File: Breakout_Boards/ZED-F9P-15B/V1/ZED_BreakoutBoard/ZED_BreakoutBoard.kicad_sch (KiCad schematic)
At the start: 15 parts, among them IC1 ZED-F9P-15B, J1 RF2-04A-T-00-50-G, J2 GPS_Conn_02x04_Top_Bottom

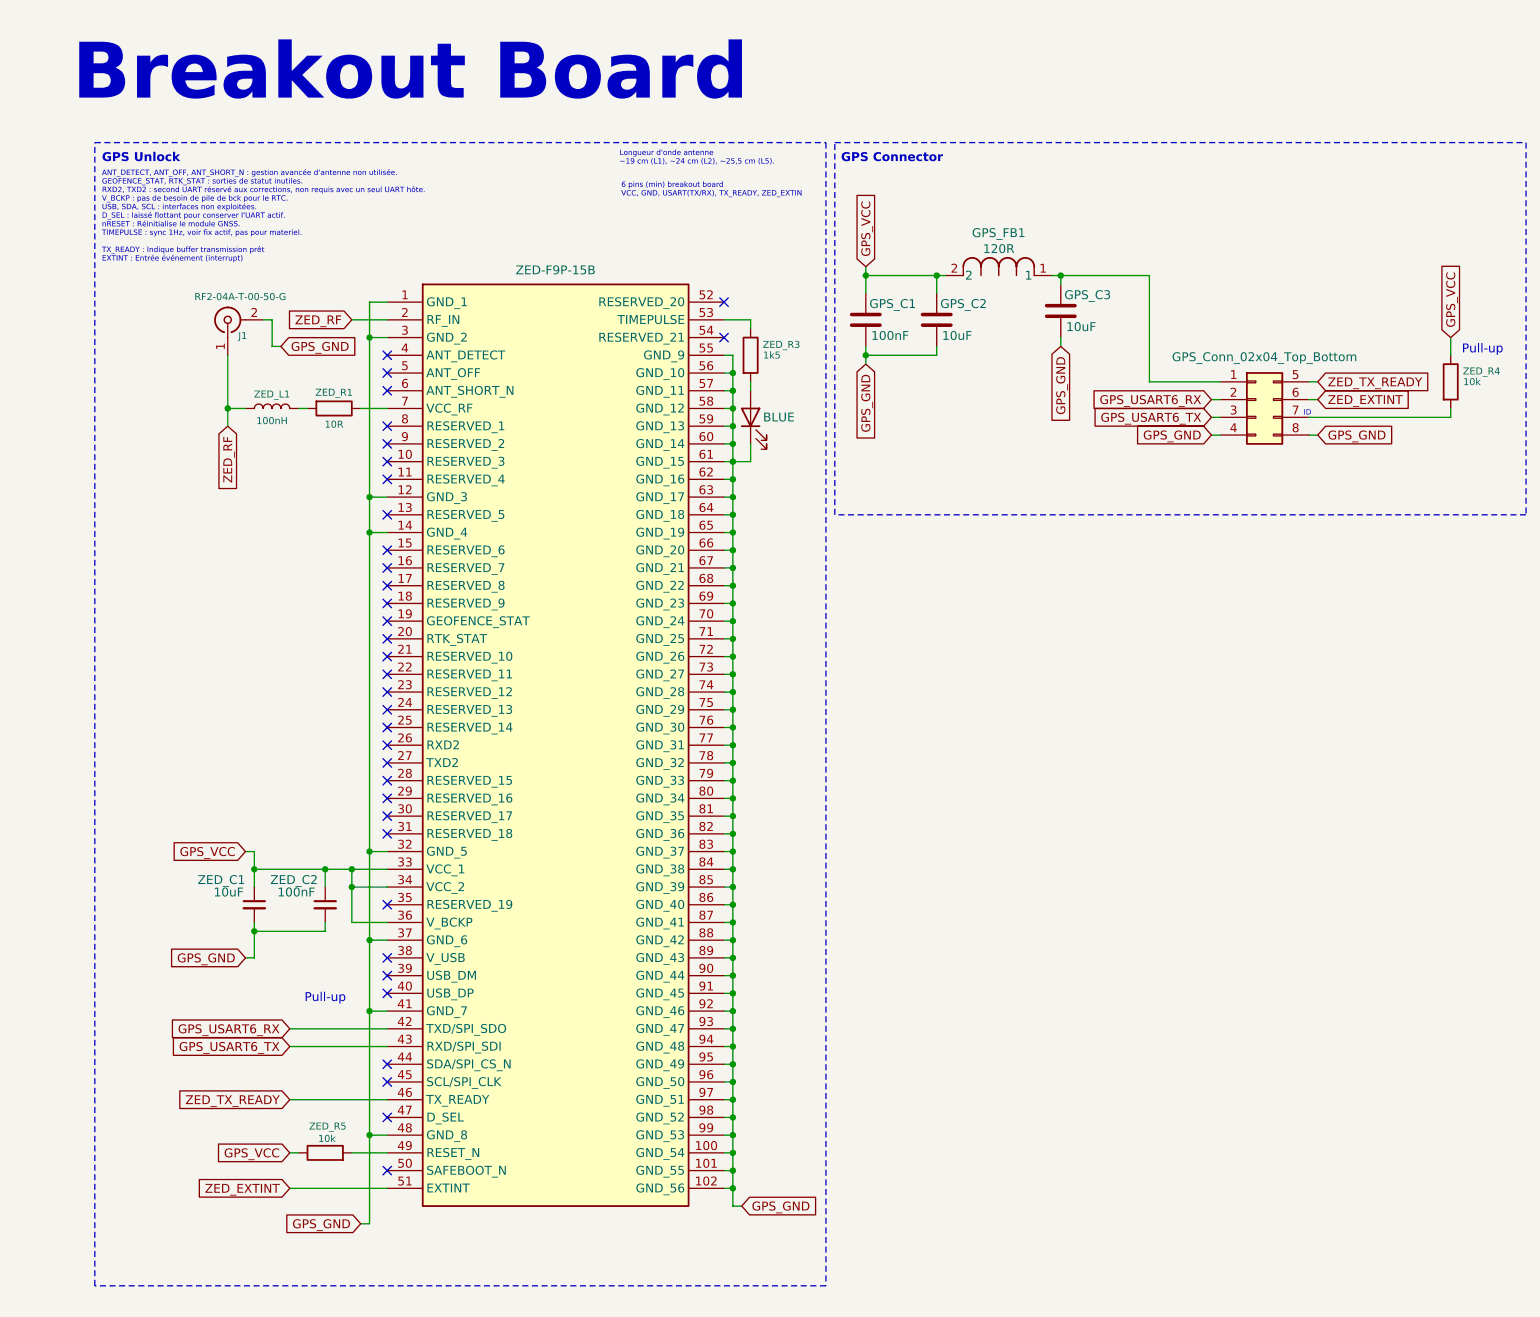
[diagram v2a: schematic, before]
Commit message: feat edge pcb sma, add edge pcb layout
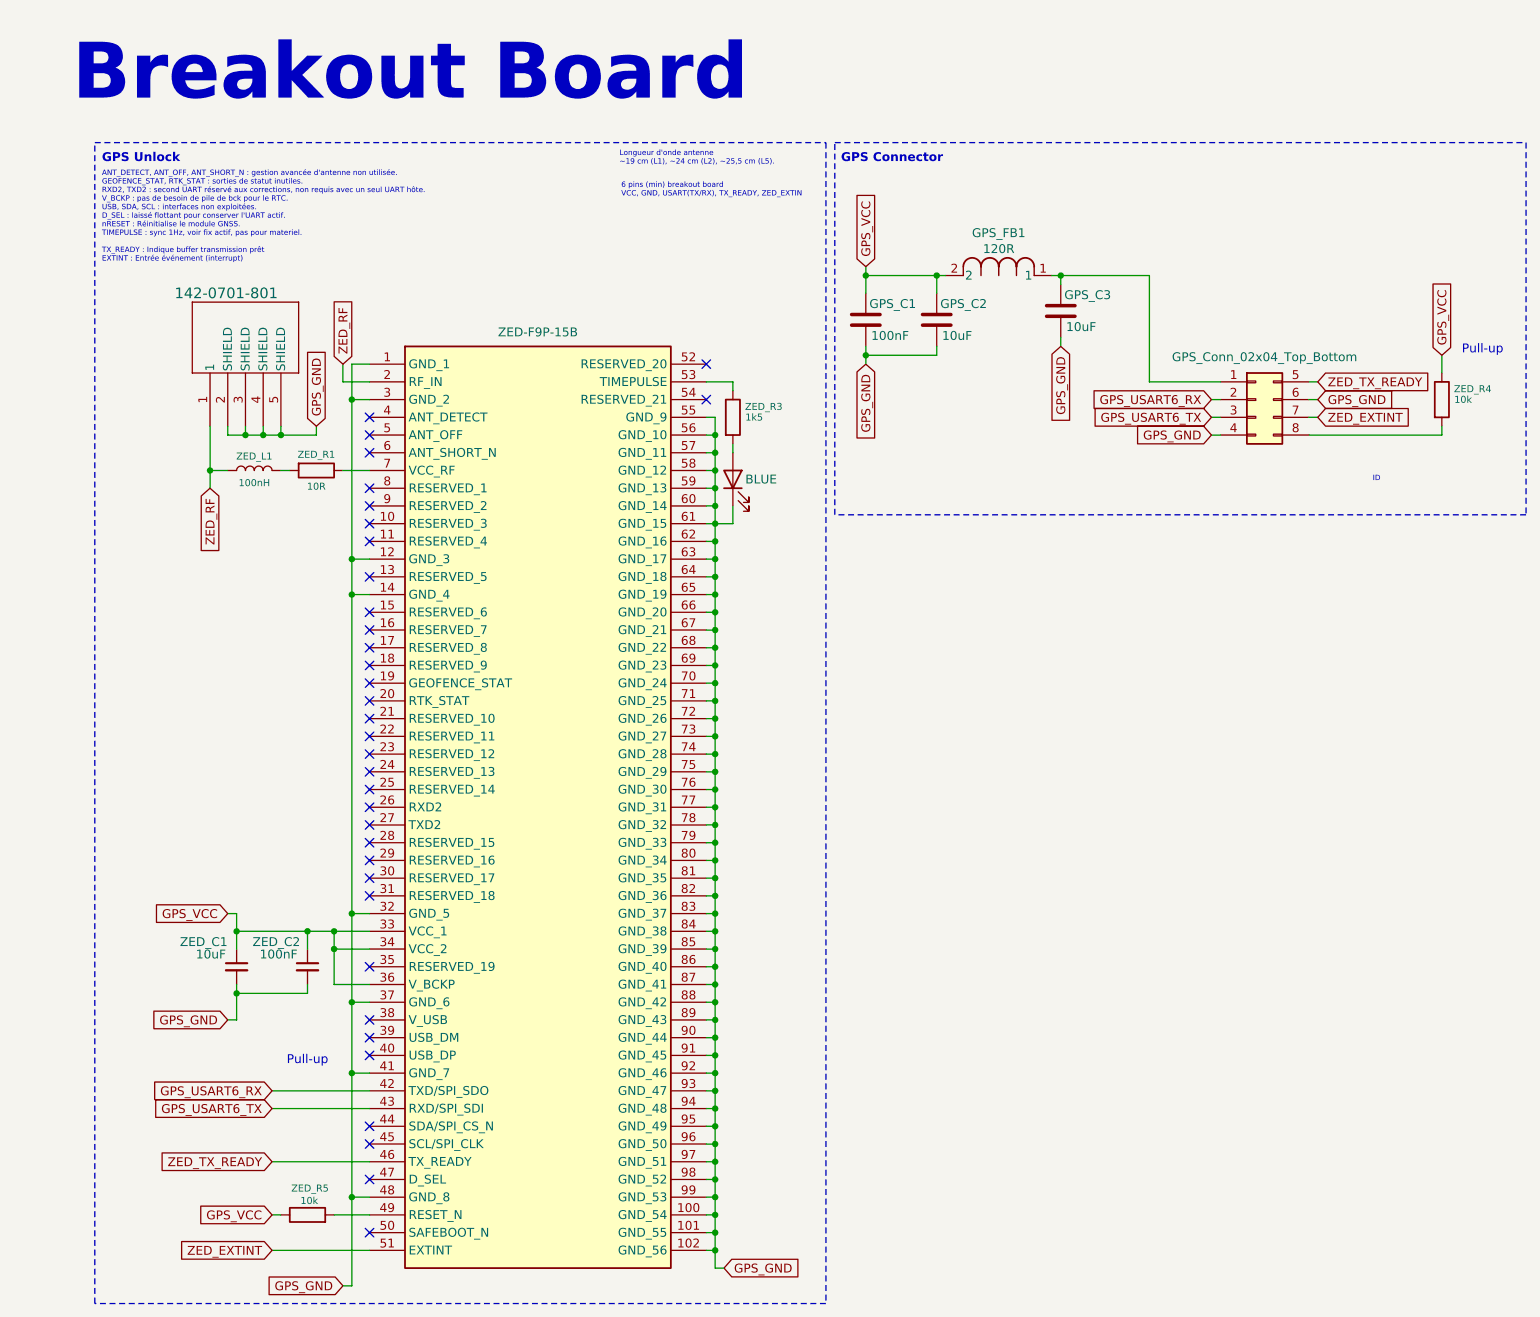
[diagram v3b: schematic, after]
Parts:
- removed J1: RF2-04A-T-00-50-G, Connector_Coaxial:SMA_Wurth_60312002114503_Vertical, symbol Connector:Conn_Coaxial
- added J1: 142-0701-801, CONN_142-0701-801, symbol ZED_Library:142-0701-801
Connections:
- net GPS_GND: now also J2.6 (Pin_6), J1.2 (SHIELD), J1.3 (SHIELD), J1.4 (SHIELD), J1.5 (SHIELD); no longer J2.8 (Pin_8)
- net ZED_EXTINT: now also J2.7 (Pin_7); no longer J2.6 (Pin_6)
- net ZED_RF: now also J1.1
- net at ZED_R4.2: now also J2.8 (Pin_8); no longer J2.7 (Pin_7)
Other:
- moved on the sheet: ZED_C1, ZED_C2, ZED_L1, ZED_R1, ZED_R3, ZED_R4, ZED_R5

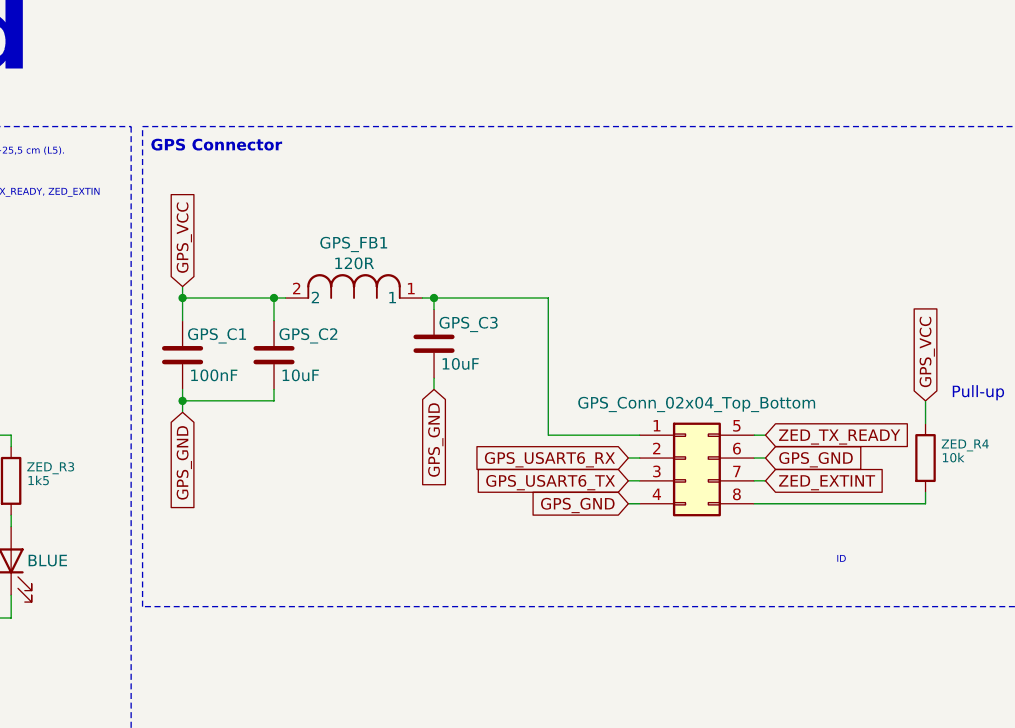
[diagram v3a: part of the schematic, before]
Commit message: fix: switch ferrite bead filtre, add gps connector to main
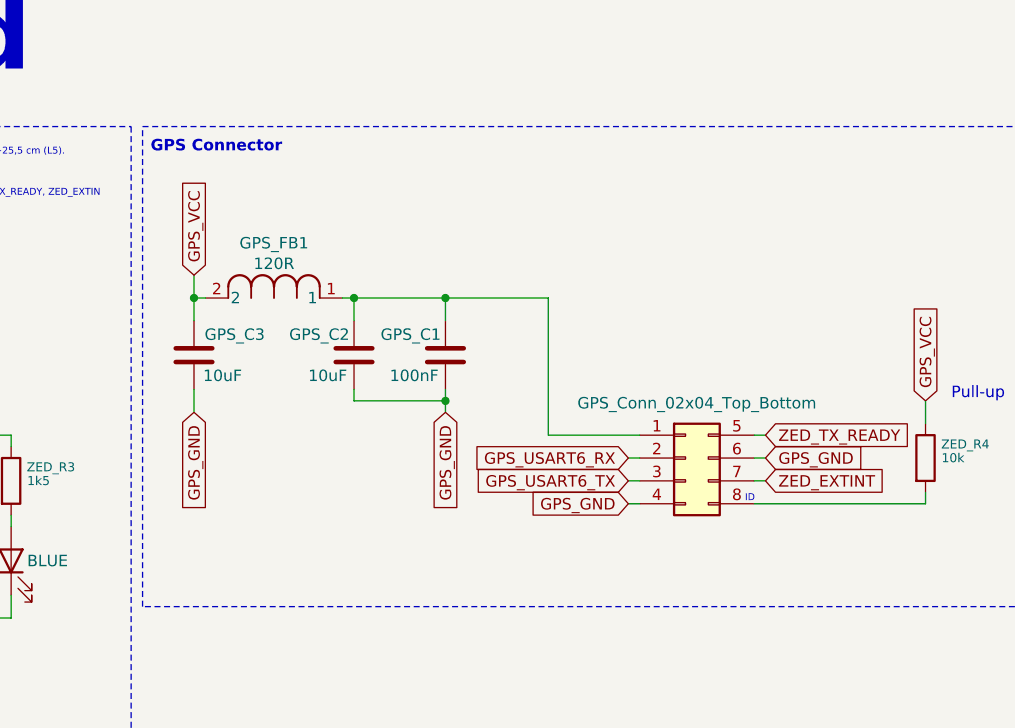
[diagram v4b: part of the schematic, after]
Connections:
- net GPS_VCC: now also GPS_C3.1; no longer GPS_C1.1, GPS_C2.1
- net at GPS_FB1.1, J2.1 (Pin_1): now also GPS_C1.1, GPS_C2.1; no longer GPS_C3.1
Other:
- moved on the sheet: GPS_C1, GPS_C2, GPS_C3, GPS_FB1
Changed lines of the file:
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@@
 	(text "ID"
 		(exclude_from_sim no)
-		(at 198.374 78.74 0)
+		(at 188.214 71.882 0)
 		(effects
 			(font
@@
 	)
 	(junction
-		(at 125.73 49.53)
-		(diameter 0)
-		(color 0 0 0 0)
-	)
-	(junction
 		(at 104.14 186.69)
 		(diameter 0)
@@
 	)
 	(junction
-		(at 125.73 60.96)
+		(at 154.94 60.96)
 		(diameter 0)
 		(color 0 0 0 0)
@@
 	)
 	(junction
+		(at 127 49.53)
+		(diameter 0)
+		(color 0 0 0 0)
+	)
+	(junction
+		(at 154.94 49.53)
+		(diameter 0)
+		(color 0 0 0 0)
+	)
+	(junction
 		(at 104.14 100.33)
 		(diameter 0)
@@
 	)
 	(junction
+		(at 144.78 49.53)
+		(diameter 0)
+		(color 0 0 0 0)
+	)
+	(junction
 		(at 104.14 128.27)
 		(diameter 0)
@@
 	)
 	(junction
-		(at 153.67 49.53)
-		(diameter 0)
-		(color 0 0 0 0)
-	)
-	(junction
 		(at 41.91 72.39)
 		(diameter 0)
@@
 	)
 	(junction
-		(at 135.89 49.53)
-		(diameter 0)
-		(color 0 0 0 0)
-	)
-	(junction
 		(at 52.07 140.97)
 		(diameter 0)
@@
 	(wire
 		(pts
-			(xy 125.73 60.96) (xy 125.73 62.23)
+			(xy 154.94 60.96) (xy 154.94 62.23)
 		)
 		(stroke
@@
 	(wire
 		(pts
-			(xy 153.67 58.42) (xy 153.67 59.69)
+			(xy 127 59.69) (xy 127 62.23)
 		)
 		(stroke
@@
 	(wire
 		(pts
+			(xy 143.51 49.53) (xy 144.78 49.53)
+		)
+		(stroke
+			(width 0)
+			(type default)
+		)
+	)
+	(wire
+		(pts
 			(xy 104.14 179.07) (xy 104.14 181.61)
 		)
@@
 	(wire
 		(pts
-			(xy 135.89 49.53) (xy 137.16 49.53)
-		)
-		(stroke
-			(width 0)
-			(type default)
-		)
-	)
-	(wire
-		(pts
 			(xy 104.14 168.91) (xy 104.14 171.45)
 		)
@@
 	(wire
 		(pts
+			(xy 154.94 49.53) (xy 166.37 49.53)
+		)
+		(stroke
+			(width 0)
+			(type default)
+		)
+	)
+	(wire
+		(pts
 			(xy 104.14 107.95) (xy 104.14 110.49)
 		)
@@
 	(wire
 		(pts
-			(xy 125.73 49.53) (xy 135.89 49.53)
+			(xy 154.94 49.53) (xy 144.78 49.53)
 		)
 		(stroke
@@
 	(wire
 		(pts
-			(xy 125.73 60.96) (xy 135.89 60.96)
+			(xy 154.94 60.96) (xy 144.78 60.96)
 		)
 		(stroke
@@
 	(wire
 		(pts
-			(xy 125.73 48.26) (xy 125.73 49.53)
-		)
-		(stroke
-			(width 0)
-			(type default)
-		)
-	)
-	(wire
-		(pts
 			(xy 52.07 67.31) (xy 52.07 90.17)
 		)
@@
 	(wire
 		(pts
-			(xy 153.67 49.53) (xy 153.67 50.8)
+			(xy 127 49.53) (xy 127 52.07)
 		)
 		(stroke
@@
 	(wire
 		(pts
-			(xy 135.89 60.96) (xy 135.89 59.69)
+			(xy 127 49.53) (xy 128.27 49.53)
+		)
+		(stroke
+			(width 0)
+			(type default)
+		)
+	)
+	(wire
+		(pts
+			(xy 144.78 60.96) (xy 144.78 59.69)
 		)
 		(stroke
@@
 	(wire
 		(pts
-			(xy 153.67 49.53) (xy 166.37 49.53)
-		)
-		(stroke
-			(width 0)
-			(type default)
-		)
-	)
-	(wire
-		(pts
 			(xy 104.14 95.25) (xy 104.14 97.79)
 		)
@@
 	(wire
 		(pts
-			(xy 104.14 77.47) (xy 104.14 74.93)
+			(xy 127 46.99) (xy 127 49.53)
 		)
 		(stroke
@@
 	(wire
 		(pts
-			(xy 152.4 49.53) (xy 153.67 49.53)
+			(xy 104.14 77.47) (xy 104.14 74.93)
 		)
 		(stroke
@@
 	(wire
 		(pts
-			(xy 125.73 49.53) (xy 125.73 52.07)
+			(xy 154.94 49.53) (xy 154.94 52.07)
 		)
 		(stroke
@@
 	(wire
 		(pts
-			(xy 125.73 59.69) (xy 125.73 60.96)
+			(xy 154.94 59.69) (xy 154.94 60.96)
 		)
 		(stroke
@@
 	(wire
 		(pts
-			(xy 135.89 49.53) (xy 135.89 52.07)
+			(xy 144.78 49.53) (xy 144.78 52.07)
 		)
 		(stroke
@@
 	(global_label "GPS_VCC"
 		(shape input)
-		(at 125.73 48.26 90)
+		(at 127 46.99 90)
 		(fields_autoplaced yes)
 		(effects
@@
 		)
 		(property "Intersheetrefs" "${INTERSHEET_REFS}"
-			(at 125.73 36.9291 90)
+			(at 127 35.6591 90)
 			(effects
 				(font
@@
 	(global_label "GPS_GND"
 		(shape input)
-		(at 153.67 59.69 270)
+		(at 127 62.23 270)
 		(fields_autoplaced yes)
 		(effects
@@
 		)
 		(property "Intersheetrefs" "${INTERSHEET_REFS}"
-			(at 153.67 71.2628 90)
+			(at 127 73.8028 90)
 			(effects
 				(font
@@
 	(global_label "GPS_GND"
 		(shape input)
-		(at 125.73 62.23 270)
+		(at 154.94 62.23 270)
 		(fields_autoplaced yes)
 		(effects
@@
 		)
 		(property "Intersheetrefs" "${INTERSHEET_REFS}"
-			(at 125.73 73.8028 90)
+			(at 154.94 73.8028 90)
 			(effects
 				(font
@@
 	(symbol
 		(lib_id "Device:C")
-		(at 153.67 54.61 0)
+		(at 127 55.88 0)
+		(mirror y)
 		(unit 1)
 		(exclude_from_sim no)
@@
 		(dnp no)
 		(property "Reference" "GPS_C3"
-			(at 154.178 52.324 0)
+			(at 134.874 53.594 0)
 			(effects
 				(font
@@
 		)
 		(property "Value" "10uF"
-			(at 154.432 56.896 0)
+			(at 132.334 58.166 0)
 			(effects
 				(font
@@
 		)
 		(property "Footprint" "Capacitor_SMD:C_0603_1608Metric"
-			(at 154.6352 58.42 0)
+			(at 126.0348 59.69 0)
 			(effects
 				(font
@@
 		)
 		(property "Datasheet" "~"
-			(at 153.67 54.61 0)
+			(at 127 55.88 0)
 			(effects
 				(font
@@
 		)
 		(property "Description" "Unpolarized capacitor"
-			(at 153.67 54.61 0)
+			(at 127 55.88 0)
 			(effects
 				(font
@@
 	(symbol
 		(lib_id "Device:C")
-		(at 135.89 55.88 0)
+		(at 144.78 55.88 0)
+		(mirror y)
 		(unit 1)
 		(exclude_from_sim no)
@@
 		(dnp no)
 		(property "Reference" "GPS_C2"
-			(at 136.398 53.594 0)
+			(at 144.272 53.594 0)
 			(effects
 				(font
@@
 		)
 		(property "Value" "10uF"
-			(at 136.652 58.166 0)
+			(at 144.018 58.166 0)
 			(effects
 				(font
@@
 		)
 		(property "Footprint" "Capacitor_SMD:C_0603_1608Metric"
-			(at 136.8552 59.69 0)
+			(at 143.8148 59.69 0)
 			(effects
 				(font
@@
 		)
 		(property "Datasheet" "~"
-			(at 135.89 55.88 0)
+			(at 144.78 55.88 0)
 			(effects
 				(font
@@
 		)
 		(property "Description" "Unpolarized capacitor"
-			(at 135.89 55.88 0)
+			(at 144.78 55.88 0)
 			(effects
 				(font
@@
 	(symbol
 		(lib_id "ZED_Library:2508051217Y6")
-		(at 137.16 49.53 0)
+		(at 128.27 49.53 0)
 		(unit 1)
 		(exclude_from_sim no)
@@
 		(dnp no)
 		(property "Reference" "GPS_FB1"
-			(at 144.78 43.434 0)
+			(at 135.89 43.434 0)
 			(effects
 				(font
@@
 		)
 		(property "Value" "120R"
-			(at 144.78 45.72 0)
+			(at 135.89 45.72 0)
 			(effects
 				(font
@@
 		)
 		(property "Footprint" "ZED_Library:IND_25_0805_FRT"
-			(at 137.16 49.53 0)
+			(at 128.27 49.53 0)
 			(effects
 				(font
@@
 		)
 		(property "Datasheet" "2508051217Y6"
-			(at 137.16 49.53 0)
+			(at 128.27 49.53 0)
 			(effects
 				(font
@@
 		)
 		(property "Description" ""
-			(at 137.16 49.53 0)
+			(at 128.27 49.53 0)
 			(effects
 				(font
@@
 	(symbol
 		(lib_id "Device:C")
-		(at 125.73 55.88 0)
+		(at 154.94 55.88 0)
+		(mirror y)
 		(unit 1)
 		(exclude_from_sim no)
@@
 		(dnp no)
 		(property "Reference" "GPS_C1"
-			(at 126.238 53.594 0)
+			(at 154.432 53.594 0)
 			(effects
 				(font
@@
 		)
 		(property "Value" "100nF"
-			(at 126.492 58.166 0)
+			(at 154.178 58.166 0)
 			(effects
 				(font
@@
 		)
 		(property "Footprint" "Capacitor_SMD:C_0603_1608Metric"
-			(at 126.6952 59.69 0)
+			(at 153.9748 59.69 0)
 			(effects
 				(font
@@
 		)
 		(property "Datasheet" "~"
-			(at 125.73 55.88 0)
+			(at 154.94 55.88 0)
 			(effects
 				(font
@@
 		)
 		(property "Description" "Unpolarized capacitor"
-			(at 125.73 55.88 0)
+			(at 154.94 55.88 0)
 			(effects
 				(font
